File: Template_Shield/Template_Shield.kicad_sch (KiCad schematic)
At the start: 4 parts

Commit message: added connector footprints
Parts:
- AD0: footprint (none) -> arduino_shield:1X06-TH-PRESSFIT
- IOH0: footprint (none) -> arduino_shield:1X10-TH-PRESSFIT
- IOL0, POWER0: footprint (none) -> arduino_shield:1X08-TH-PRESSFIT
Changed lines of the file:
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@@
 			)
 		)
-		(property "Footprint" ""
+		(property "Footprint" "arduino_shield:1X08-TH-PRESSFIT"
 			(at 185.42 20.32 0)
 			(effects
@@
 			)
 		)
-		(property "Footprint" ""
+		(property "Footprint" "arduino_shield:1X10-TH-PRESSFIT"
 			(at 154.94 20.32 0)
 			(effects
@@
 			)
 		)
-		(property "Footprint" ""
+		(property "Footprint" "arduino_shield:1X08-TH-PRESSFIT"
 			(at 170.18 160.02 0)
 			(effects
@@
 			)
 		)
-		(property "Footprint" ""
+		(property "Footprint" "arduino_shield:1X06-TH-PRESSFIT"
 			(at 193.04 160.02 0)
 			(effects

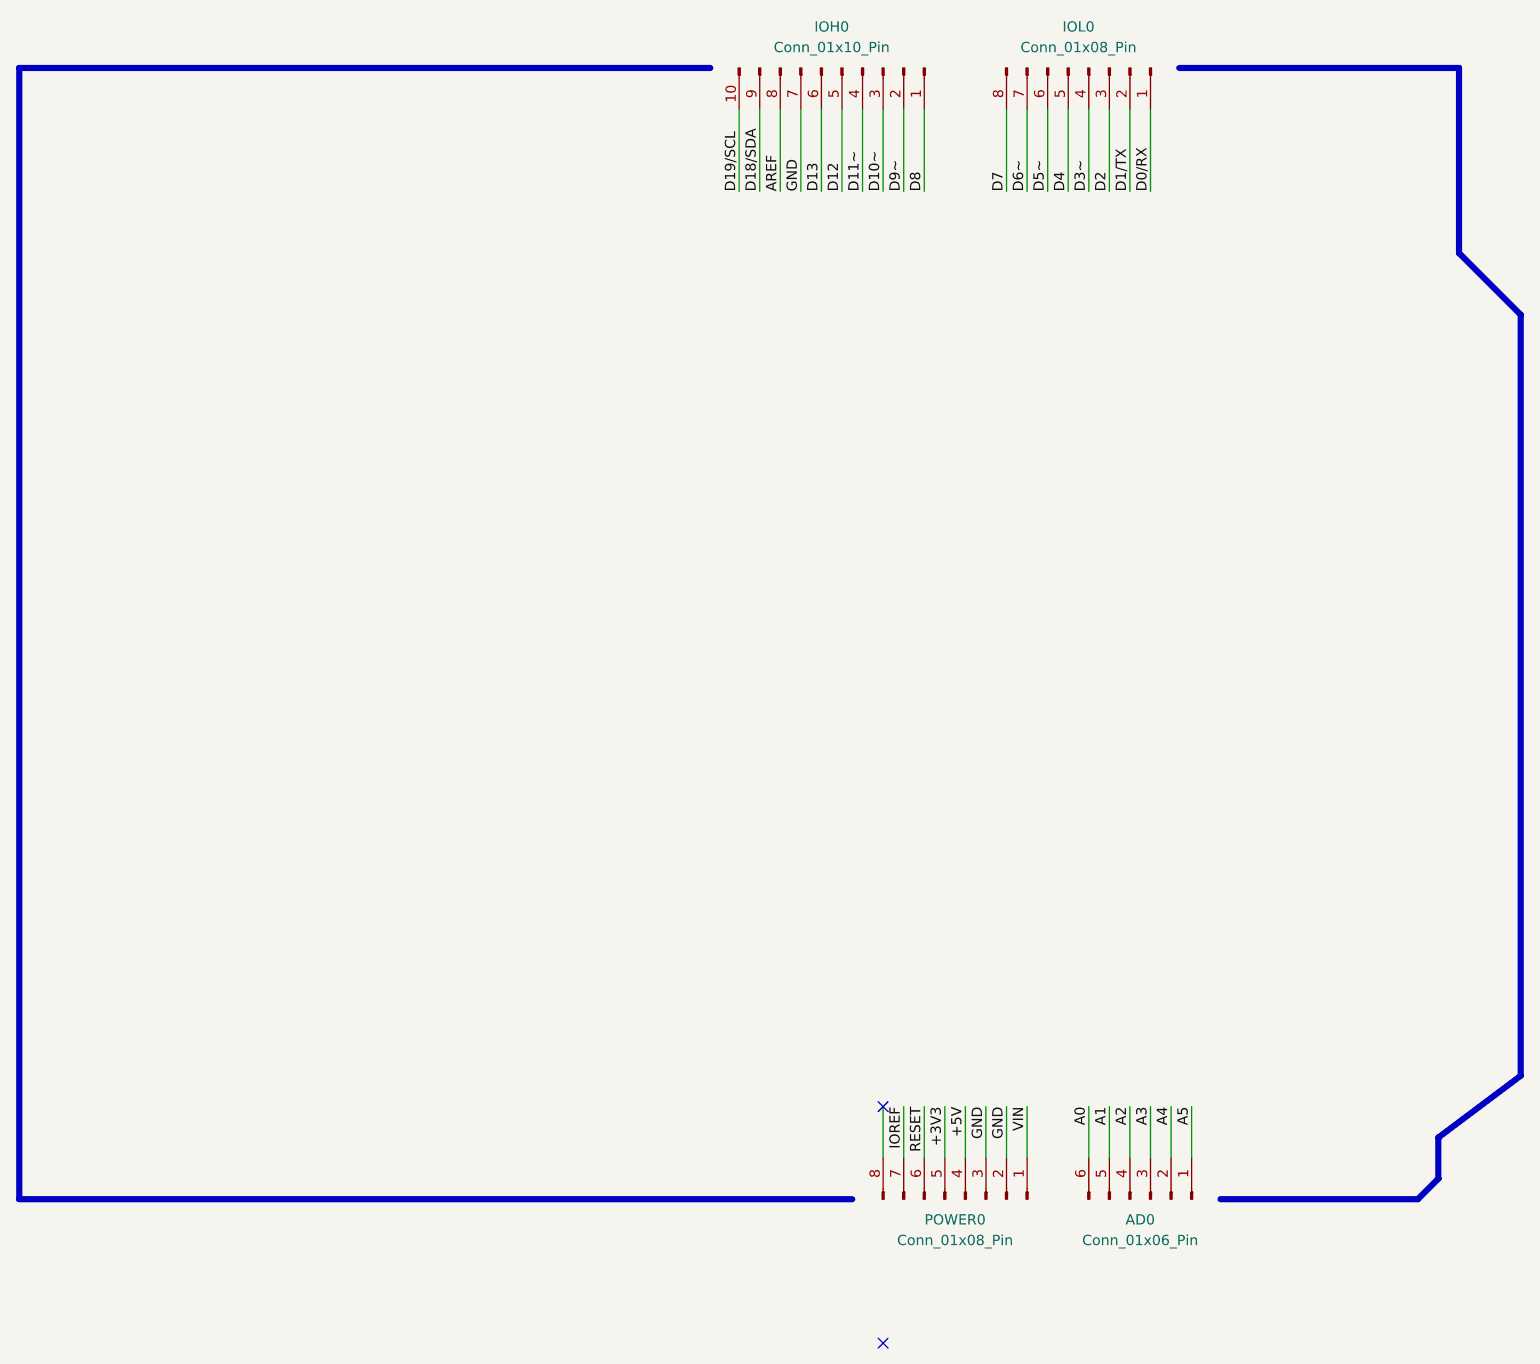
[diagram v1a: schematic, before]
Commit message: added datasheet and header models to PCB
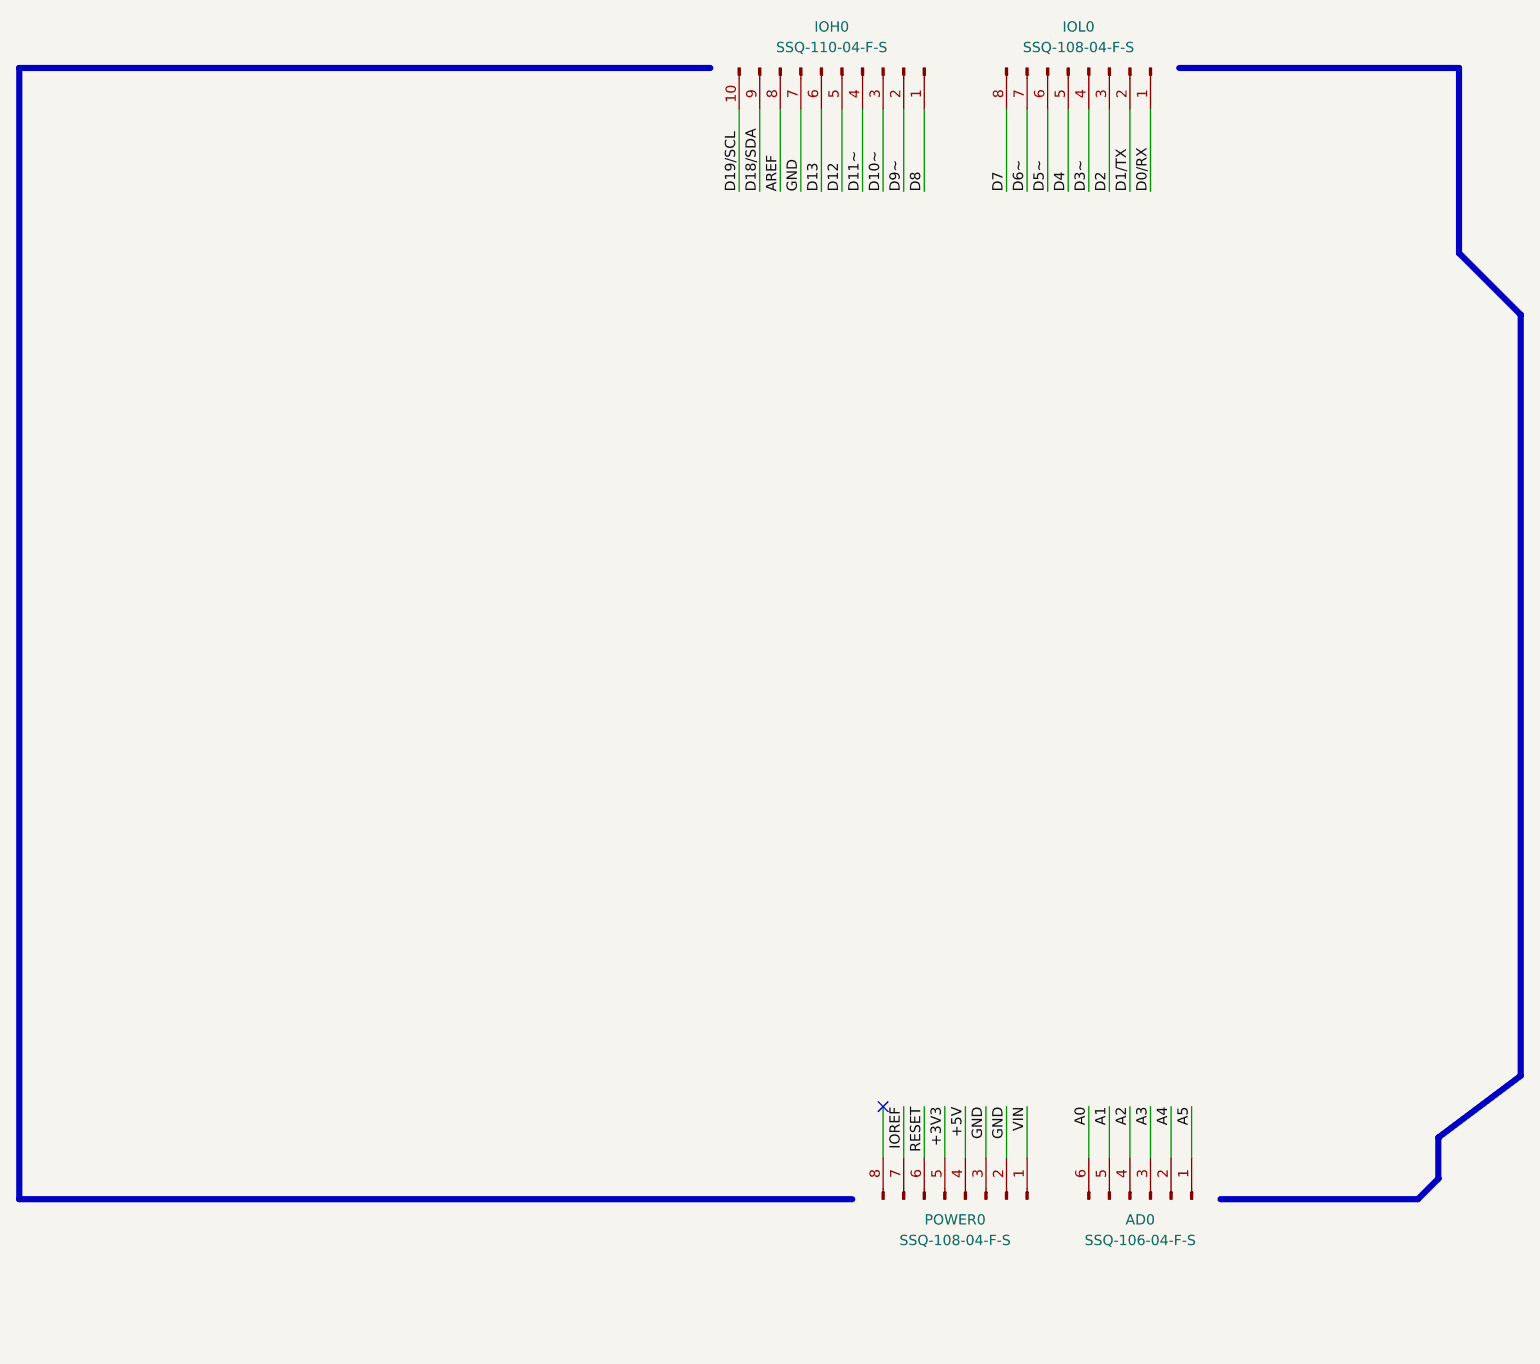
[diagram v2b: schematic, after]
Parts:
- AD0: value Conn_01x06_Pin -> SSQ-106-04-F-S
- IOH0: value Conn_01x10_Pin -> SSQ-110-04-F-S
- IOL0, POWER0: value Conn_01x08_Pin -> SSQ-108-04-F-S
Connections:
- no-connect marks 2 -> 1
